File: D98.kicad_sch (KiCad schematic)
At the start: 15 parts, among them J1 Conn_01x02, J2 Conn_01x04, J3 Conn_01x08, J4 Conn_01x06, J5 Conn_01x06, J6 Conn_01x06, J7 Conn_01x05, U1 SRV05-4, U2 YAAJ_BluePill_SWD_Breakout, U3 Poka Yoke

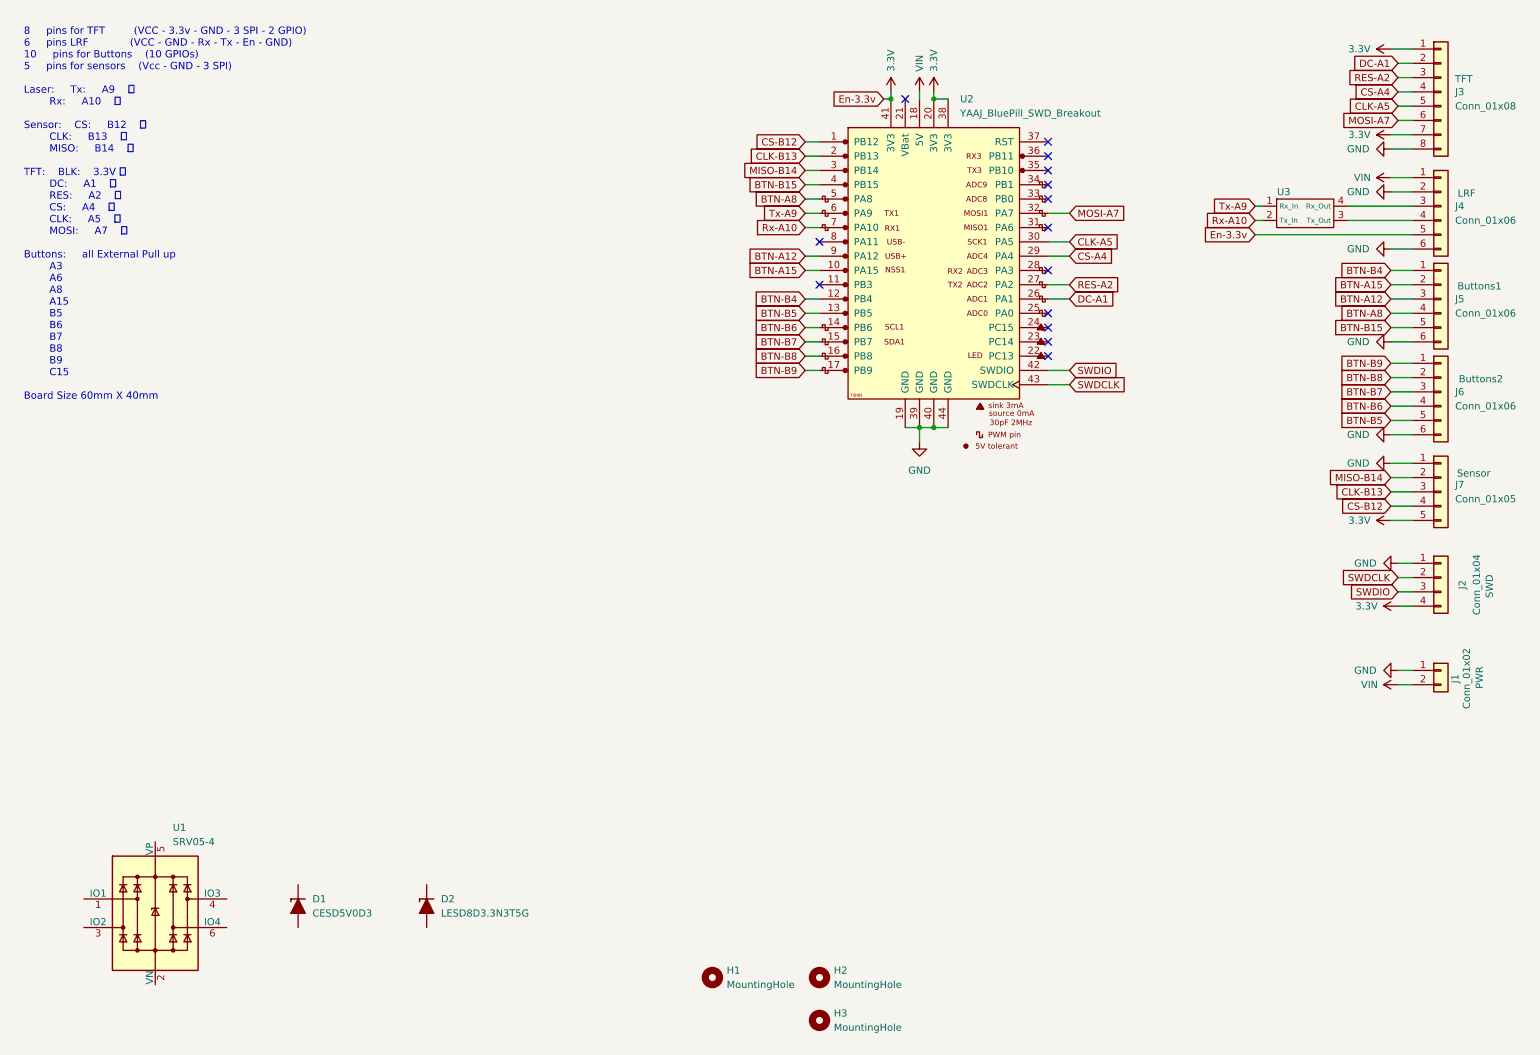
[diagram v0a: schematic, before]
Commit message: feat: 	changed position of MountingHoles             Small modefication and Rounding Tracks.
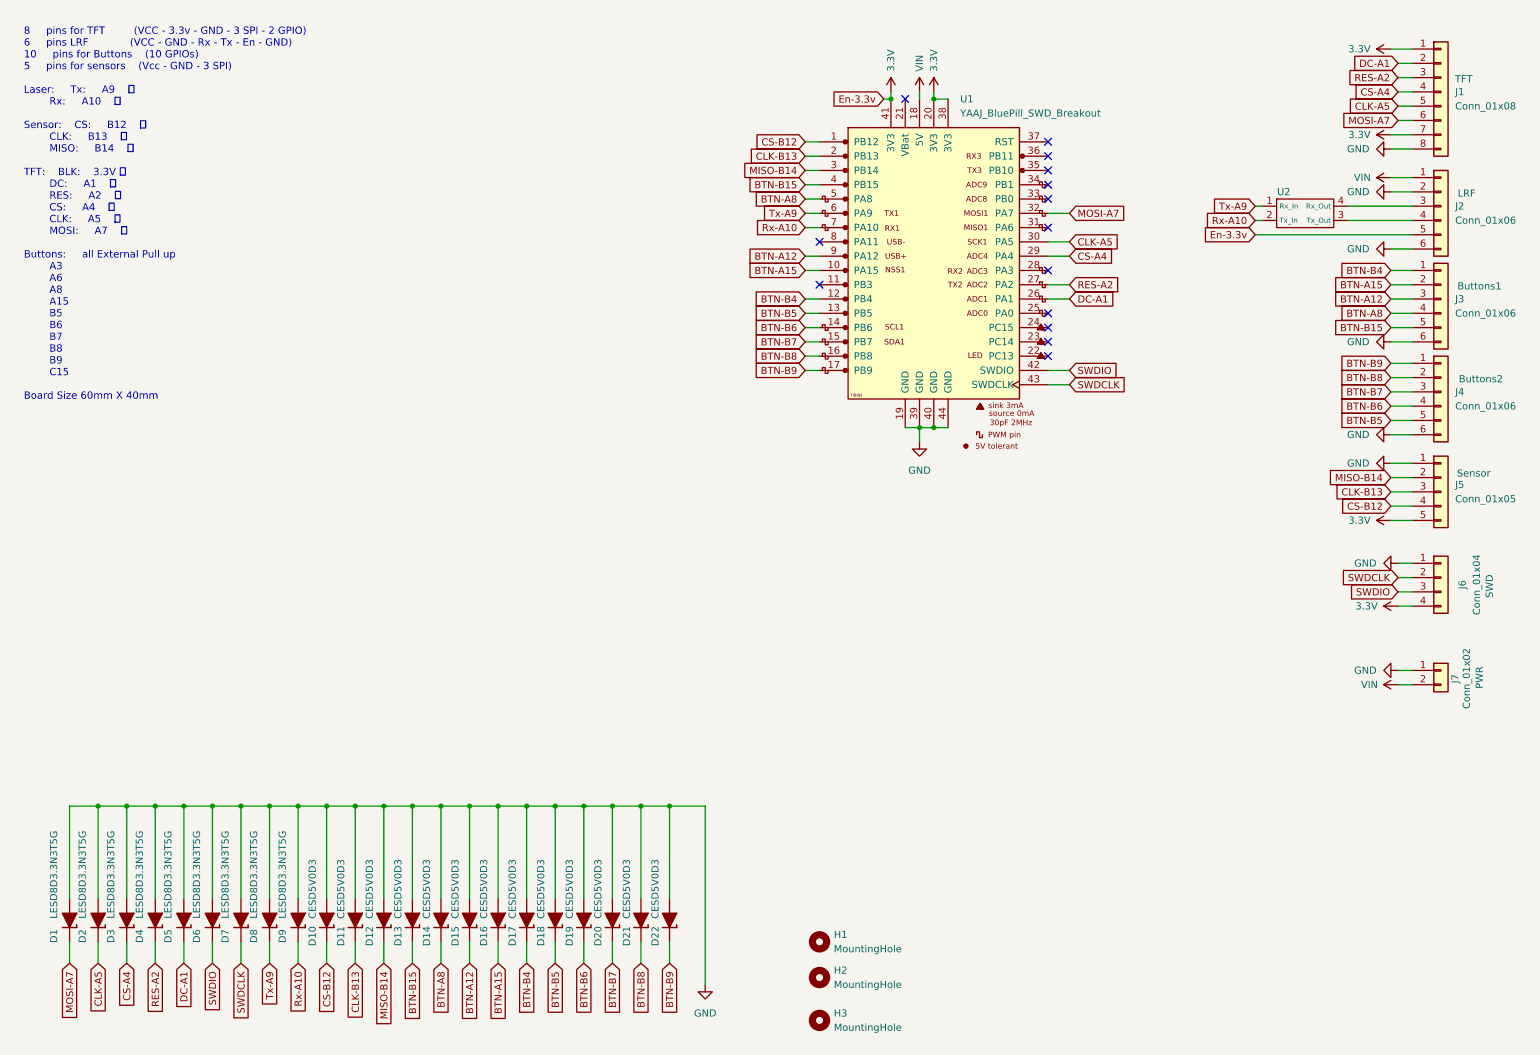
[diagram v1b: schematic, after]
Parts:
- removed U1: SRV05-4, Package_TO_SOT_SMD:SOT-23-6, symbol Power_Protection:SRV05-4
- added D11, D12, D13, D14, D15, D16, D17, D18, D19, D20, D21, D22: CESD5V0D3, Diode_SMD:D_SOD-323_HandSoldering, symbol Diode:D_TVS_Unidirectional_Generic
- added D2, D3, D4, D5, D6, D7, D8, D9: LESD8D3.3N3T5G, Diode_SMD:D_SOD-882D, symbol PCM_Diode_TVS_AKL:LESD8D3.3CAT5G
- D1: renamed from D2; LINK (none) -> https://makerselectronics.com/product/esd-smd-tvs-sod-882-3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
- renumbered D1 to D10, J3 to J1, J4 to J2, J5 to J3, J6 to J4, J7 to J5, J2 to J6, J1 to J7, U2 to U1, U3 to U2
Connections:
- net BTN-A12: now also D15.1 (K)
- net BTN-A15: now also D16.1 (K)
- net BTN-A8: now also D14.1 (K)
- net BTN-B15: now also D13.1 (K)
- net BTN-B4: now also D17.1 (K)
- net BTN-B5: now also D18.1 (K)
- net BTN-B6: now also D19.1 (K)
- net BTN-B7: now also D20.1 (K)
- net BTN-B8: now also D21.1 (K)
- net BTN-B9: now also D22.1 (K)
- net CLK-A5: now also D2.1 (K)
- net CLK-B13: now also D11.1 (K)
- net CS-A4: now also D3.1 (K)
- net CS-B12: now also D10.1 (K)
- net DC-A1: now also D5.1 (K)
- net GND: now also D1.2 (A), D10.2 (A), D11.2 (A), D12.2 (A), D13.2 (A), D14.2 (A), D15.2 (A), D16.2 (A), D17.2 (A), D18.2 (A), D19.2 (A), D2.2 (A), D20.2 (A), D21.2 (A), D22.2 (A), D3.2 (A), D4.2 (A), D5.2 (A), D6.2 (A), D7.2 (A), D8.2 (A), D9.2 (A)
- net MISO-B14: now also D12.1 (K)
- net MOSI-A7: now also D1.1 (K)
- net RES-A2: now also D4.1 (K)
- net Rx-A10: now also D9.1 (K)
- net SWDCLK: now also D7.1 (K)
- net SWDIO: now also D6.1 (K)
- net Tx-A9: now also D8.1 (K)
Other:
- moved on the sheet: D1, D10, H1

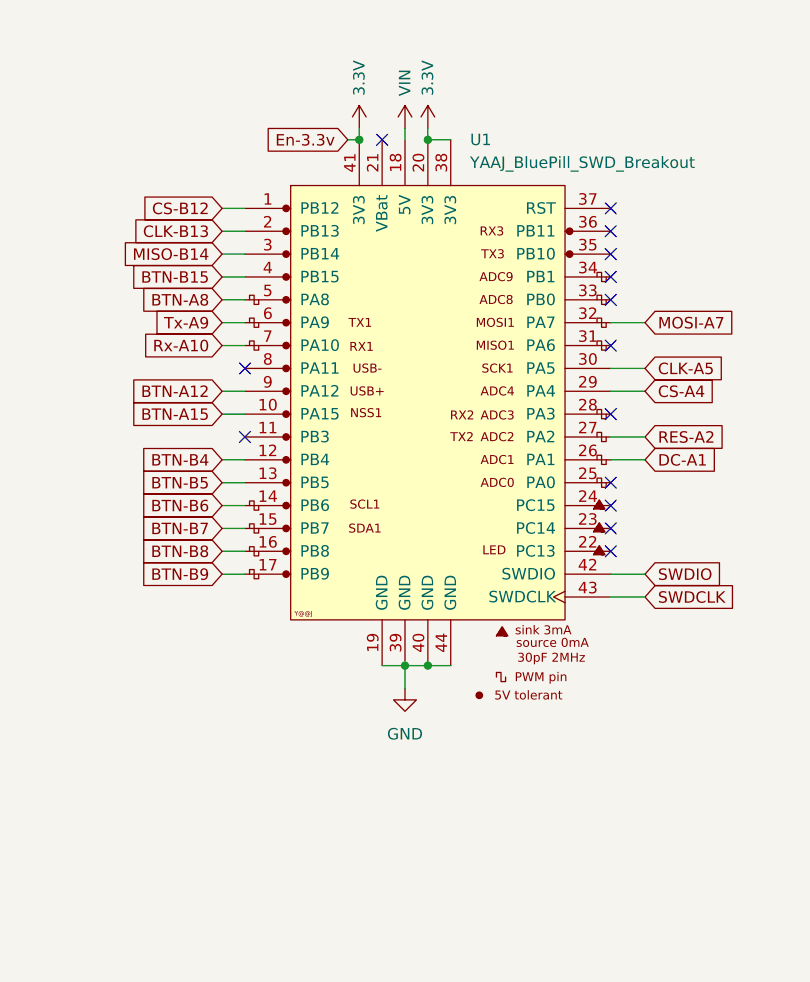
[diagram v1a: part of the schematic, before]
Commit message: Fix:  -SWD pins wasn't installed correctlly now the connection is correct. 		-adding some pin assignment in the back side.
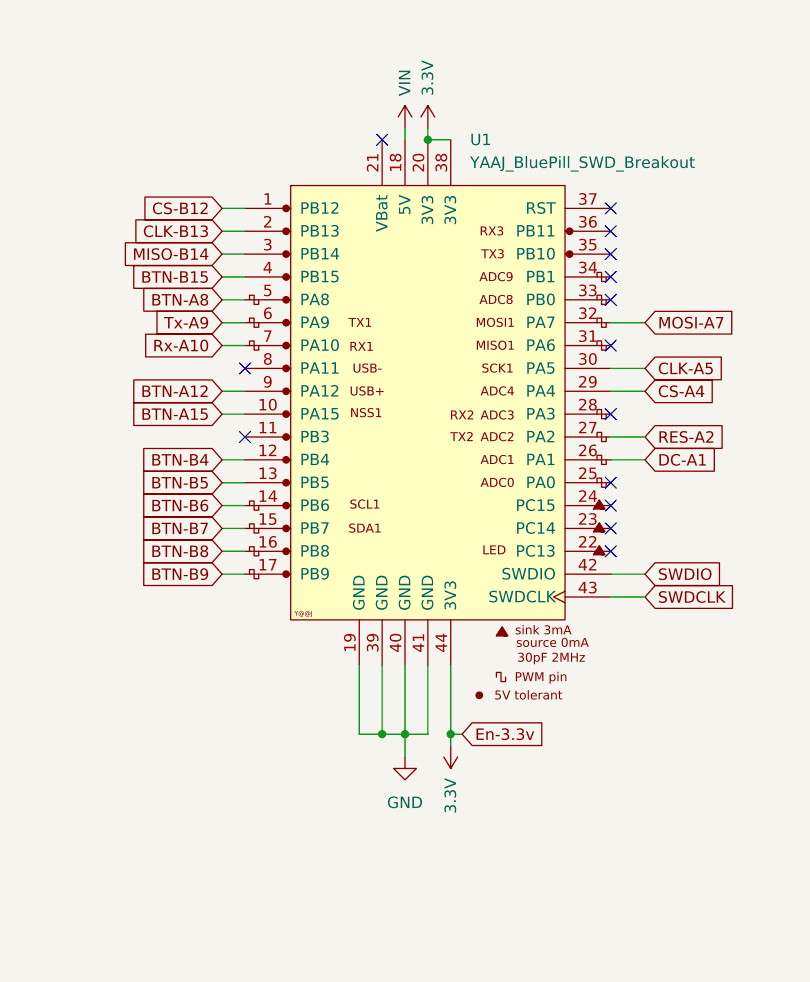
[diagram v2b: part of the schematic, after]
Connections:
- net 3.3V: now also U1.44 (3V3); no longer U1.41 (3V3)
- net GND: now also U1.41 (GND); no longer U1.44 (GND)
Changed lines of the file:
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@@
 	)
 	(junction
+		(at 173.99 93.98)
+		(diameter 0)
+		(color 0 0 0 0)
+	)
+	(junction
 		(at 38.1 153.67)
 		(diameter 0)
@@
 	)
 	(junction
-		(at 173.99 86.36)
+		(at 43.18 153.67)
 		(diameter 0)
 		(color 0 0 0 0)
 	)
 	(junction
-		(at 43.18 153.67)
+		(at 171.45 93.98)
 		(diameter 0)
 		(color 0 0 0 0)
@@
 	)
 	(junction
-		(at 176.53 86.36)
-		(diameter 0)
-		(color 0 0 0 0)
-	)
-	(junction
 		(at 73.66 153.67)
 		(diameter 0)
@@
 	)
 	(junction
-		(at 168.91 27.94)
+		(at 179.07 93.98)
 		(diameter 0)
 		(color 0 0 0 0)
@@
 	(wire
 		(pts
-			(xy 173.99 86.36) (xy 176.53 86.36)
+			(xy 173.99 93.98) (xy 176.53 93.98)
 		)
 		(stroke
@@
 	(wire
 		(pts
+			(xy 171.45 86.36) (xy 171.45 93.98)
+		)
+		(stroke
+			(width 0)
+			(type default)
+		)
+	)
+	(wire
+		(pts
 			(xy 73.66 181.61) (xy 73.66 177.8)
 		)
@@
 	(wire
 		(pts
+			(xy 168.91 86.36) (xy 168.91 93.98)
+		)
+		(stroke
+			(width 0)
+			(type default)
+		)
+	)
+	(wire
+		(pts
 			(xy 58.42 153.67) (xy 63.5 153.67)
 		)
@@
 	(wire
 		(pts
-			(xy 176.53 86.36) (xy 179.07 86.36)
+			(xy 250.19 46.99) (xy 261.62 46.99)
 		)
 		(stroke
@@
 	(wire
 		(pts
-			(xy 250.19 46.99) (xy 261.62 46.99)
+			(xy 104.14 153.67) (xy 109.22 153.67)
 		)
 		(stroke
@@
 	(wire
 		(pts
-			(xy 104.14 153.67) (xy 109.22 153.67)
+			(xy 73.66 153.67) (xy 78.74 153.67)
 		)
 		(stroke
@@
 	(wire
 		(pts
-			(xy 73.66 153.67) (xy 78.74 153.67)
+			(xy 124.46 181.61) (xy 124.46 177.8)
 		)
 		(stroke
@@
 	(wire
 		(pts
-			(xy 124.46 181.61) (xy 124.46 177.8)
+			(xy 257.81 80.01) (xy 261.62 80.01)
 		)
 		(stroke
@@
 	(wire
 		(pts
-			(xy 257.81 80.01) (xy 261.62 80.01)
+			(xy 168.91 93.98) (xy 171.45 93.98)
 		)
 		(stroke
@@
 	(wire
 		(pts
-			(xy 173.99 88.9) (xy 173.99 86.36)
+			(xy 173.99 96.52) (xy 173.99 93.98)
+		)
+		(stroke
+			(width 0)
+			(type default)
+		)
+	)
+	(wire
+		(pts
+			(xy 173.99 86.36) (xy 173.99 93.98)
 		)
 		(stroke
@@
 	(wire
 		(pts
+			(xy 176.53 93.98) (xy 176.53 86.36)
+		)
+		(stroke
+			(width 0)
+			(type default)
+		)
+	)
+	(wire
+		(pts
 			(xy 33.02 153.67) (xy 38.1 153.67)
 		)
@@
 	(wire
 		(pts
-			(xy 171.45 86.36) (xy 173.99 86.36)
+			(xy 171.45 93.98) (xy 173.99 93.98)
 		)
 		(stroke
@@
 	(wire
 		(pts
-			(xy 168.91 26.67) (xy 168.91 27.94)
+			(xy 179.07 95.25) (xy 179.07 93.98)
 		)
 		(stroke
@@
 	(wire
 		(pts
-			(xy 167.64 27.94) (xy 168.91 27.94)
+			(xy 180.34 93.98) (xy 179.07 93.98)
 		)
 		(stroke
@@
 		)
 	)
+	(wire
+		(pts
+			(xy 179.07 86.36) (xy 179.07 93.98)
+		)
+		(stroke
+			(width 0)
+			(type default)
+		)
+	)
 	(global_label "BTN-B5"
 		(shape input)
@@
 	(global_label "En-3.3v"
 		(shape input)
-		(at 167.64 27.94 180)
+		(at 180.34 93.98 0)
 		(fields_autoplaced yes)
 		(effects
@@
 				(size 1.27 1.27)
 			)
-			(justify right)
+			(justify left)
 		)
 		(property "Intersheetrefs" "${INTERSHEET_REFS}"
-			(at 156.793 27.94 0)
+			(at 191.187 93.98 0)
 			(effects
 				(font
 					(size 1.27 1.27)
 				)
-				(justify right)
+				(justify left)
 				(hide yes)
 			)
@@
 	(symbol
 		(lib_id "SparkFun-PowerSymbol:3.3V")
-		(at 168.91 26.67 0)
+		(at 179.07 95.25 180)
 		(unit 1)
 		(exclude_from_sim no)
@@
 		(dnp no)
 		(property "Reference" "#PWR02"
-			(at 168.91 30.48 0)
+			(at 179.07 91.44 0)
 			(effects
 				(font
@@
 		)
 		(property "Value" "3.3V"
-			(at 168.91 21.082 90)
+			(at 179.07 100.838 90)
 			(do_not_autoplace yes)
 			(effects
@@
 		)
 		(property "Footprint" ""
-			(at 168.91 26.67 0)
+			(at 179.07 95.25 0)
 			(effects
 				(font
@@
 		)
 		(property "Datasheet" ""
-			(at 168.91 26.67 0)
+			(at 179.07 95.25 0)
 			(effects
 				(font
@@
 		)
 		(property "Description" "Power symbol creates a global label with name \"3.3V\""
-			(at 168.91 33.02 0)
+			(at 179.07 88.9 0)
 			(effects
 				(font
@@
 	(symbol
 		(lib_id "power:GND")
-		(at 173.99 88.9 0)
+		(at 173.99 96.52 0)
 		(unit 1)
 		(exclude_from_sim no)
@@
 		(fields_autoplaced yes)
 		(property "Reference" "#PWR04"
-			(at 173.99 95.25 0)
+			(at 173.99 102.87 0)
 			(effects
 				(font
@@
 		)
 		(property "Value" "GND"
-			(at 173.99 93.98 0)
+			(at 173.99 101.6 0)
 			(effects
 				(font
@@
 		)
 		(property "Footprint" ""
-			(at 173.99 88.9 0)
+			(at 173.99 96.52 0)
 			(effects
 				(font
@@
 		)
 		(property "Datasheet" ""
-			(at 173.99 88.9 0)
+			(at 173.99 96.52 0)
 			(effects
 				(font
@@
 		)
 		(property "Description" "Power symbol creates a global label with name \"GND\" , ground"
-			(at 173.99 88.9 0)
+			(at 173.99 96.52 0)
 			(effects
 				(font
